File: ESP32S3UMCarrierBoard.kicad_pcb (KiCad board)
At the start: 2 copper layers, 75.8 x 45 mm, 11 parts, among them J1 EDGES3D, J2 USB_C_Receptacle_USB2.0_16P, SW1 BOOT, SW2 RESET, U1 USBLC6-2SC6

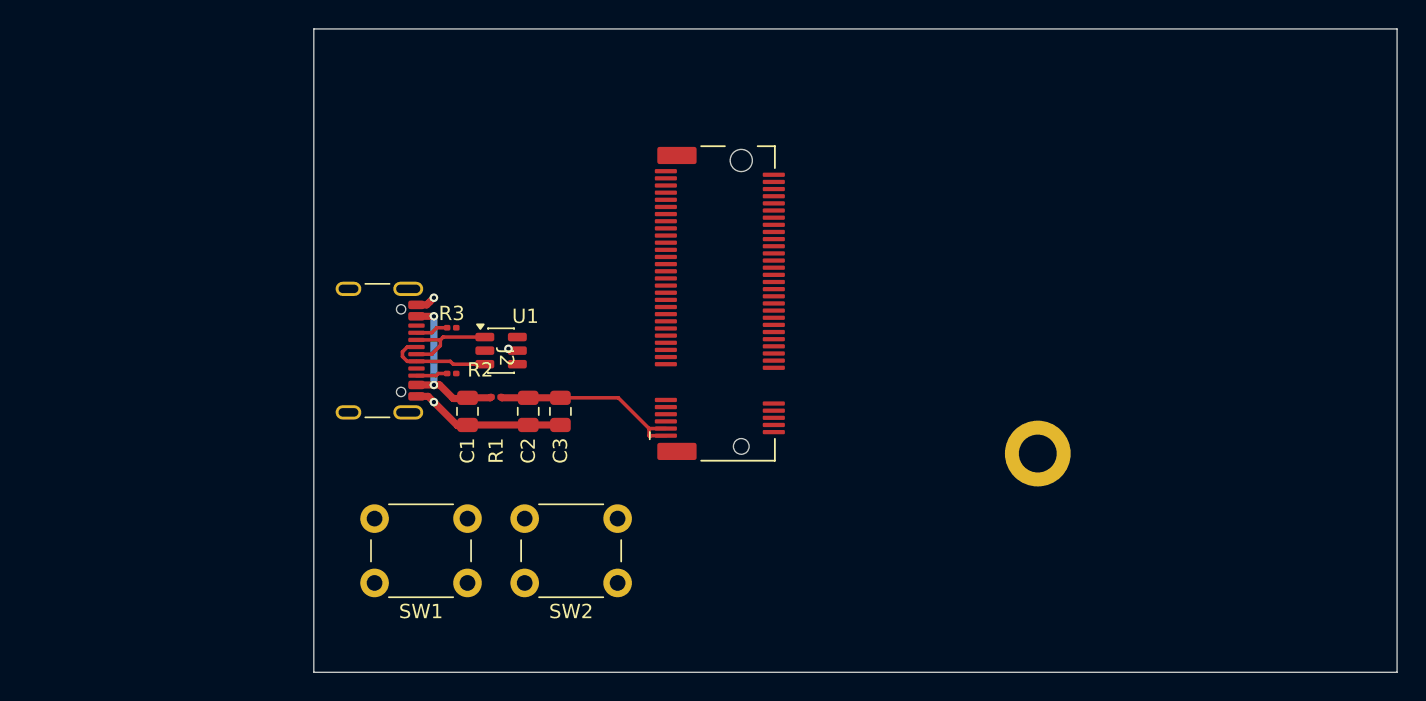
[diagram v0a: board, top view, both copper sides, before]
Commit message: Added JTAG Debugging connection Added Battery Connection
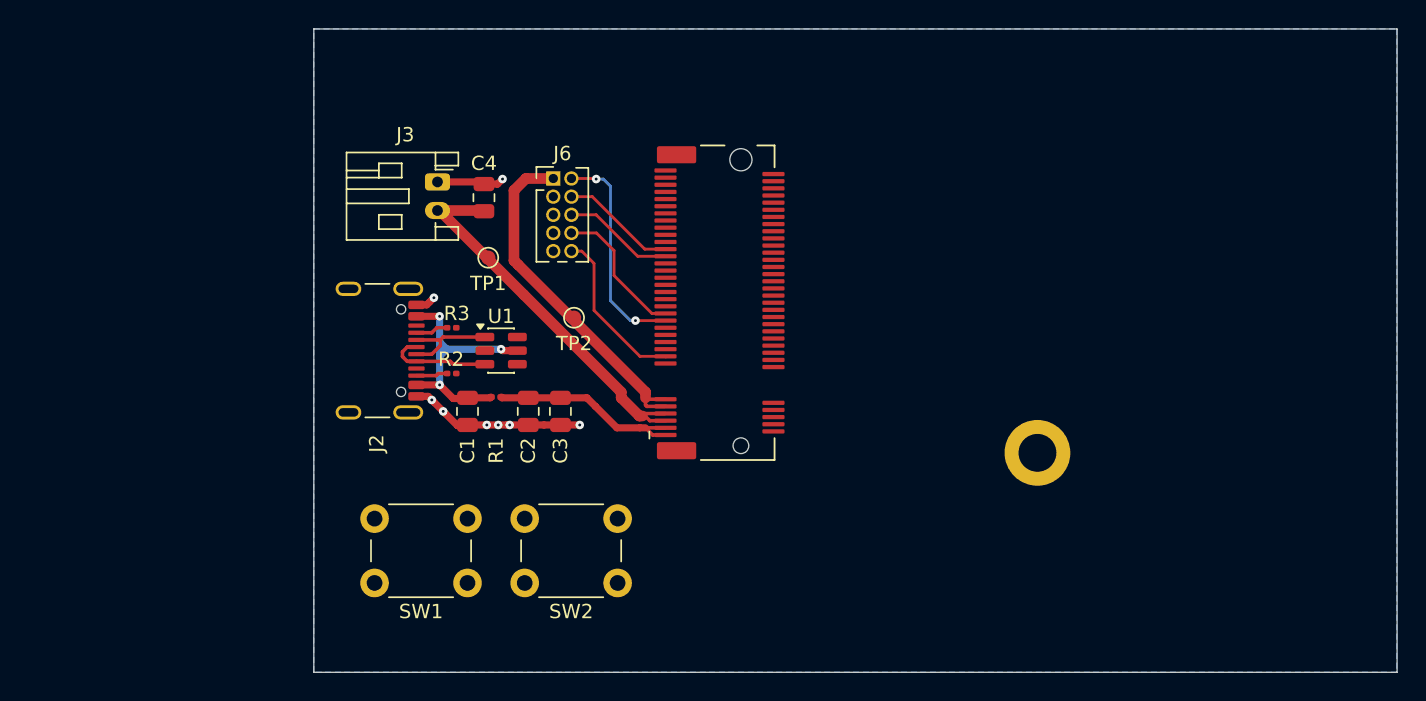
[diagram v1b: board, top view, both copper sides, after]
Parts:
- added C4: 10u, Capacitor_SMD:C_0805_2012Metric, F.Cu at (104.1, 57.0)
- added J3: Battery, Connector_JST:JST_PH_S2B-PH-K_1x02_P2.00mm_Horizontal, F.Cu at (100.9, 55.9)
- added J6: Conn_ARM_JTAG_SWD_10, Connector_PinHeader_1.27mm:PinHeader_2x05_P1.27mm_Vertical, F.Cu at (109.0, 55.7)
- added TP1: LiTo_TP_Small, TestPoint:TestPoint_Pad_D1.0mm, F.Cu at (104.4, 61.2)
- added TP2: LiTo_TP_Small, TestPoint:TestPoint_Pad_D1.0mm, F.Cu at (110.4, 65.4)
- moved J1 0.06 mm to (122.1, 64.4)
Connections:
- net Net-(J1-RESET) renamed /CarrierBoard_BlockModel/RESET
- J1 pad 29: unconnected-(J1-IO44/RX-Pad29) -> /CarrierBoard_BlockModel/U0RXD
- J1 pad 31: unconnected-(J1-IO43/TX-Pad31) -> /CarrierBoard_BlockModel/U0TXD
- J1 pad 33: unconnected-(J1-IO42/MTMS-Pad33) -> /CarrierBoard_BlockModel/JTAG_MTMS
- J1 pad 35: unconnected-(J1-IO41/MTDI-Pad35) -> /CarrierBoard_BlockModel/JTAG_MTDI
- J1 pad 51: unconnected-(J1-IO40/MTDO-Pad51) -> /CarrierBoard_BlockModel/JTAG_MTDO
- J1 pad 53: unconnected-(J1-IO39/MTCK-Pad53) -> /CarrierBoard_BlockModel/JTAG_MTCK
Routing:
- net +BATT: track 0.00 -> 27.2 mm
- net +3V3: track 0.00 -> 24.8 mm
- net /CarrierBoard_BlockModel/JTAG_MTMS: track 0.00 -> 15.4 mm, vias 0 -> 2
- net /CarrierBoard_BlockModel/RESET: track 0.00 -> 11.6 mm
- net /CarrierBoard_BlockModel/JTAG_MTDI: track 0.00 -> 9.94 mm
- net /CarrierBoard_BlockModel/JTAG_MTCK: track 0.00 -> 8.08 mm
- net /CarrierBoard_BlockModel/JTAG_MTDO: track 0.00 -> 7.78 mm
- net +VBUS: track 11.3 -> 18.7 mm
- net GND: track 12.2 -> 18.3 mm, vias 2 -> 8
- added copper zone on B.Cu, net GND

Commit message: Boardconfig update
updated board config
updated outline
moved USB and battery connections
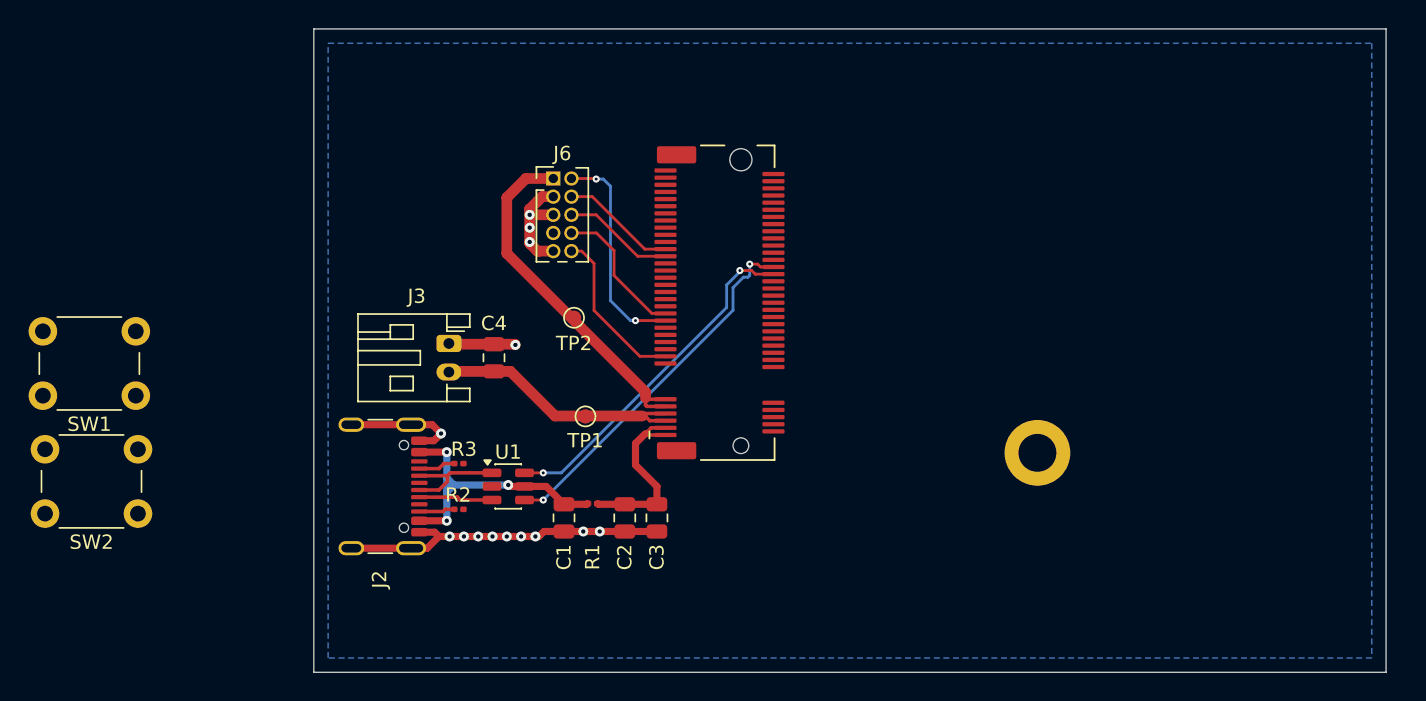
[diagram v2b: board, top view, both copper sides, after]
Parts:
- moved SW2 33.9 mm to (79.9, 79.1)
- moved SW1 26.6 mm to (79.8, 70.9)
- moved TP1 13.0 mm to (111.2, 72.3)
- moved J3 11.3 mm to (101.7, 67.2)
- moved C4 11.2 mm to (104.8, 68.2)
- moved C1 10.1 mm to (109.7, 79.4)
- moved C2 10.1 mm to (114.0, 79.4)
- moved C3 10.1 mm to (116.2, 79.4)
- moved R1 10.1 mm to (111.7, 78.4)
- moved R2 9.51 mm to (102.4, 78.8)
- moved R3 9.51 mm to (102.4, 75.6)
- moved U1 9.51 mm to (105.8, 77.2)
- moved J2 9.50 mm to (95.9, 77.2)
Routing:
- net GND: track 18.3 -> 44.1 mm, vias 8 -> 14
- net /CarrierBoard_BlockModel/USB_D+: track 0.00 -> 25.7 mm, vias 0 -> 2
- net /CarrierBoard_BlockModel/USB_D-: track 0.00 -> 24.4 mm, vias 0 -> 2
- net +BATT: track 27.2 -> 18.3 mm
- net /CarrierBoard_BlockModel/USBCD+: track 7.43 -> 6.15 mm
- net +VBUS: track 18.7 -> 19.8 mm
- net +VUSB: track 14.0 -> 13.0 mm
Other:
- board size 75.8 x 45 mm -> 75 x 45 mm
